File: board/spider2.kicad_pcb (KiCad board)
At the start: 2 copper layers, 137 x 75.5 mm, 123 parts, among them J1 NRJ6HH-1, J10 PJ-320A, J11 PJ358, J12 PJ358, J13 PJ358, J14 PJ358, J15 PJ358, J16 PJ358, J19 PJ358, J2 NRJ6HH-1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

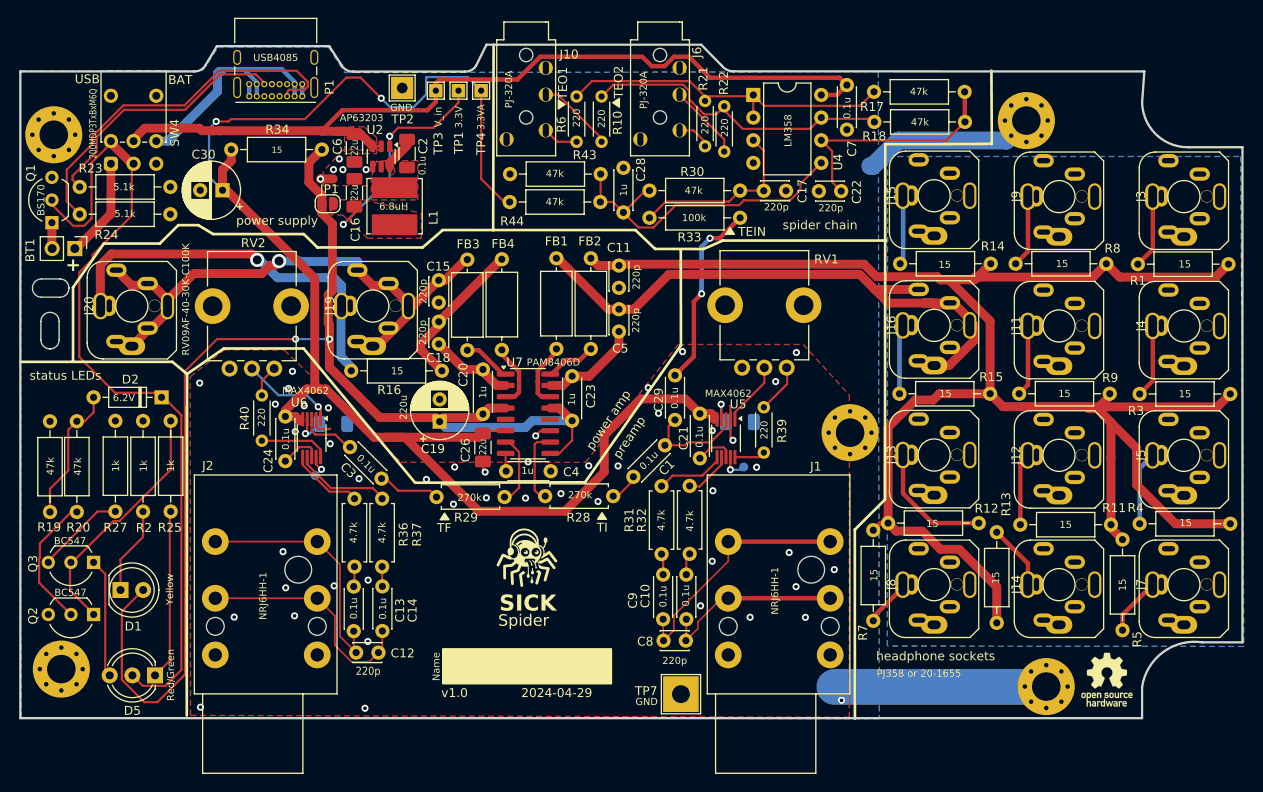
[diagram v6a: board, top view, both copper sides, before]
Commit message: silkscreen updates
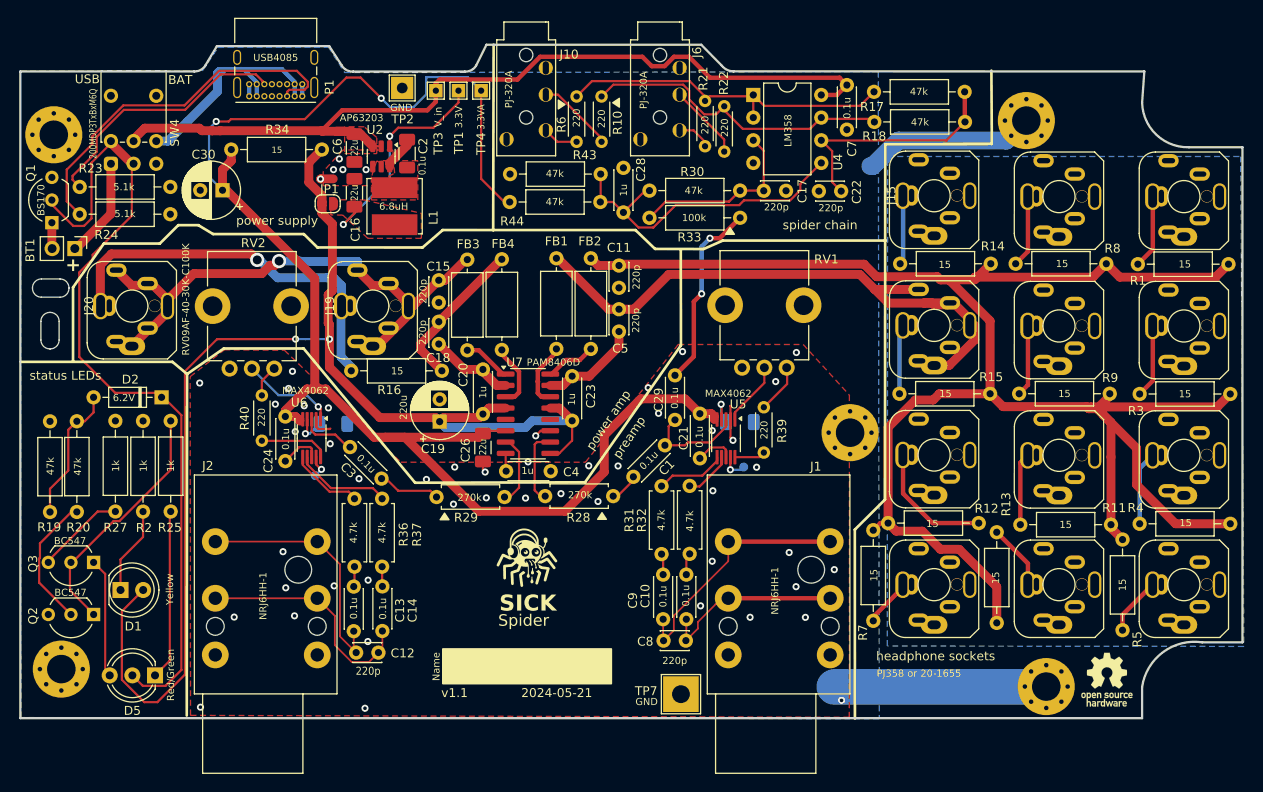
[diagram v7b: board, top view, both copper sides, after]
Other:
- board text added: "2024-05-21"
- board text added: "v1.1"
- board text removed: "2024-04-29"
- board text removed: "TEIN"
- board text removed: "TEO1"
- board text removed: "TEO2"
- board text removed: "TF"
- board text removed: "TI"
- board text removed: "v1.0"
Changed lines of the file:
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@@
 		)
 		(property "Value" "200MDP3TxBxM6Q"
-			(at 4.4934 -1.9994 270)
+			(at 4.4934 -1.9994 -90)
 			(layer "F.SilkS")
 			(effects
@@
 			(unlocked yes)
 			(layer "F.SilkS")
+			(hide yes)
 			(effects
 				(font
@@
 			(unlocked yes)
 			(layer "F.SilkS")
+			(hide yes)
 			(effects
 				(font
@@
 			(unlocked yes)
 			(layer "F.SilkS")
+			(hide yes)
 			(effects
 				(font
@@
 			(unlocked yes)
 			(layer "F.SilkS")
+			(hide yes)
 			(effects
 				(font
@@
 			(unlocked yes)
 			(layer "F.SilkS")
+			(hide yes)
 			(effects
 				(font
@@
 			(unlocked yes)
 			(layer "F.SilkS")
+			(hide yes)
 			(effects
 				(font
@@
 			(unlocked yes)
 			(layer "F.SilkS")
+			(hide yes)
 			(effects
 				(font
@@
 			(unlocked yes)
 			(layer "F.SilkS")
+			(hide yes)
 			(effects
 				(font
@@
 			(unlocked yes)
 			(layer "F.SilkS")
+			(hide yes)
 			(effects
 				(font
@@
 			(unlocked yes)
 			(layer "F.SilkS")
+			(hide yes)
 			(effects
 				(font
@@
 			(unlocked yes)
 			(layer "F.SilkS")
+			(hide yes)
 			(effects
 				(font
@@
 		)
 	)
-	(gr_text "2024-04-29"
+	(gr_text "2024-05-21"
 		(at 193.791151 100.845524 0)
 		(layer "F.SilkS")
@@
 		)
 	)
-	(gr_text "TEO1"
-		(at 199.05 33.75 90)
-		(layer "F.SilkS")
-		(effects
-			(font
-				(size 1 1)
-				(thickness 0.15)
-			)
-			(justify left bottom)
-		)
-	)
-	(gr_text "TEIN"
-		(at 218.1 49.15 0)
-		(layer "F.SilkS")
-		(effects
-			(font
-				(size 1 1)
-				(thickness 0.15)
-			)
-			(justify left bottom)
-		)
-	)
-	(gr_text "TEO2"
-		(at 205.3 33.6 90)
-		(layer "F.SilkS")
-		(effects
-			(font
-				(size 1 1)
-				(thickness 0.15)
-			)
-			(justify left bottom)
-		)
-	)
 	(gr_text "preamp\n"
 		(at 204.9 74.15 56)
@@
 		)
 	)
-	(gr_text "v1.0"
+	(gr_text "v1.1"
 		(at 184.821151 100.845524 0)
 		(layer "F.SilkS")
@@
 		)
 	)
-	(gr_text "TI"
-		(at 202.25 82.3 0)
-		(layer "F.SilkS")
-		(effects
-			(font
-				(size 1 1)
-				(thickness 0.15)
-			)
-			(justify left bottom)
-		)
-	)
 	(gr_text "headphone sockets"
 		(at 233.575 96.725 0)
@@
 			)
 			(justify left bottom)
-		)
-	)
-	(gr_text "TF"
-		(at 184.35 82.35 0)
-		(layer "F.SilkS")
-		(effects
-			(font
-				(size 1 1)
-				(thickness 0.15)
-			)
-			(justify left bottom)

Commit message: thicker traces to reduce the chance of irreparable damage by ripping them off
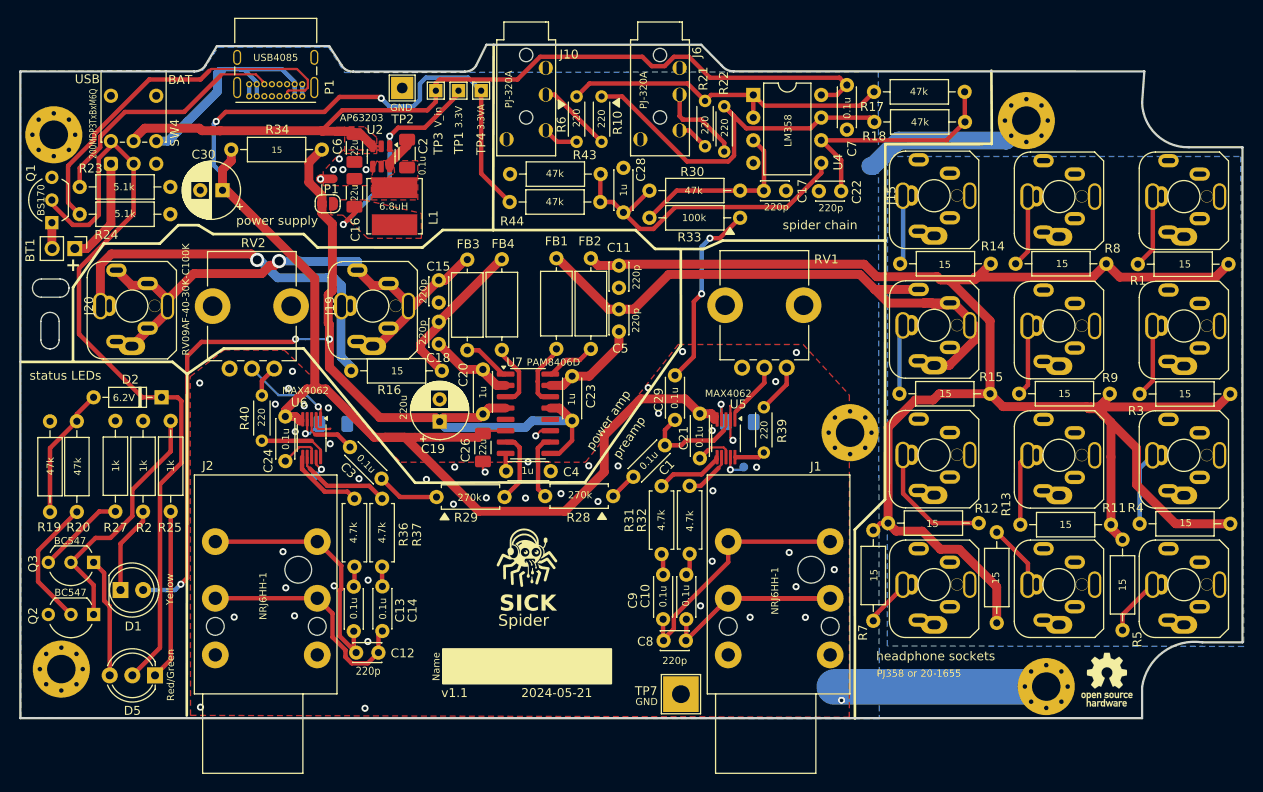
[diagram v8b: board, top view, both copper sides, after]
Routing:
- net +3.3V: track 145.1 -> 120.3 mm, vias 2 -> 3
- net /Preamp Interpreter/IN-: track 21.0 -> 32.6 mm
- net Net-(R10-Pad1): track 35.5 -> 42.7 mm
- net INT_OUT: track 11.8 -> 16.6 mm
- net +BATT: track 93.0 -> 88.8 mm
- net Net-(U5-IN-): track 5.42 -> 9.50 mm
- net +3.3VA: track 171.1 -> 168.2 mm
- net Net-(J6-PadR1): track 8.45 -> 9.65 mm
- net Net-(P1-VCONN): track 29.2 -> 28.3 mm
- net Net-(BT1-+): track 11.3 -> 12.0 mm
- net Net-(U7-INR): track 8.06 -> 7.40 mm
- net Net-(JP1-A): track 26.4 -> 25.9 mm
- net Net-(U4A--): track 39.2 -> 38.7 mm
- net Net-(D2-A): track 15.4 -> 14.9 mm
